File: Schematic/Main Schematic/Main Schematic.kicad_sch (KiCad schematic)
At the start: 7 parts, among them J1 Conn_01x24_Socket, J10 Conn_01x08_Pin, J3 Conn_01x24_Socket, J8 Conn_01x24_Pin, J9 Conn_01x24_Pin, SW1 SW_Push

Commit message: Updated the pcb
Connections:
- net RXD: now also J3.18 (Pin_18), J8.18 (Pin_18); no longer J3.19 (Pin_19), J8.19 (Pin_19)
- net TXD: now also J3.19 (Pin_19), J8.19 (Pin_19); no longer J3.18 (Pin_18), J8.18 (Pin_18)
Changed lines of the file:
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@@
     )
   )
-  (label "TXD" (at 253.9492 74.2696 0) (fields_autoplaced)
+  (label "TXD" (at 253.9492 76.8096 0) (fields_autoplaced)
     (effects (font (size 1.27 1.27)) (justify left bottom))
   )
@@
     (effects (font (size 1.27 1.27)) (justify left bottom))
   )
-  (label "RXD" (at 239.268 76.6572 0) (fields_autoplaced)
+  (label "RXD" (at 239.268 74.1172 0) (fields_autoplaced)
     (effects (font (size 1.27 1.27)) (justify left bottom))
   )
@@
     (effects (font (size 1.27 1.27)) (justify right bottom))
   )
-  (label "TXD" (at 239.268 74.1172 0) (fields_autoplaced)
-    (effects (font (size 1.27 1.27)) (justify left bottom))
-  )
-  (label "RXD" (at 253.9492 76.8096 0) (fields_autoplaced)
-    (effects (font (size 1.27 1.27)) (justify left bottom))
-  )
+  (label "TXD" (at 239.268 76.6572 0) (fields_autoplaced)
+    (effects (font (size 1.27 1.27)) (justify left bottom))
+  )
+  (label "RXD" (at 253.9492 74.2696 0) (fields_autoplaced)
+    (effects (font (size 1.27 1.27)) (justify left bottom))
+  )

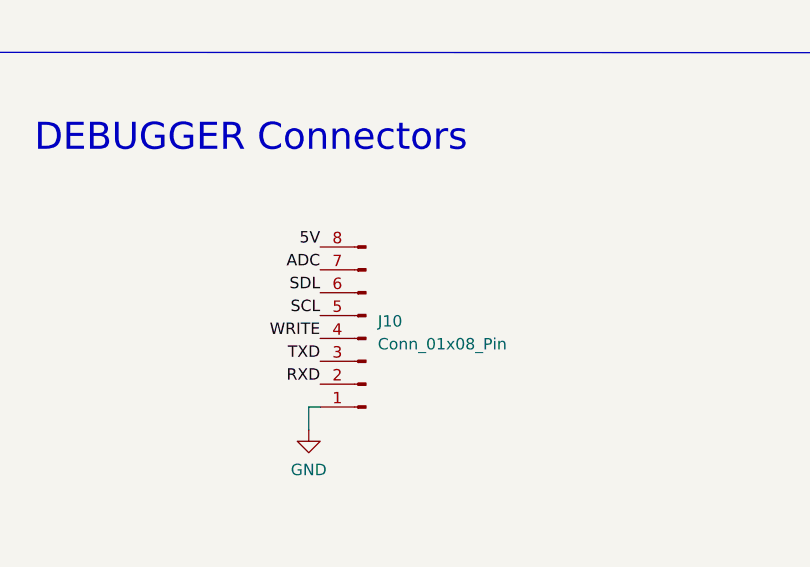
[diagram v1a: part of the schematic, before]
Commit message: Added more led for visual indications, also changed debugger pins to 9 pins for 3.3v pin
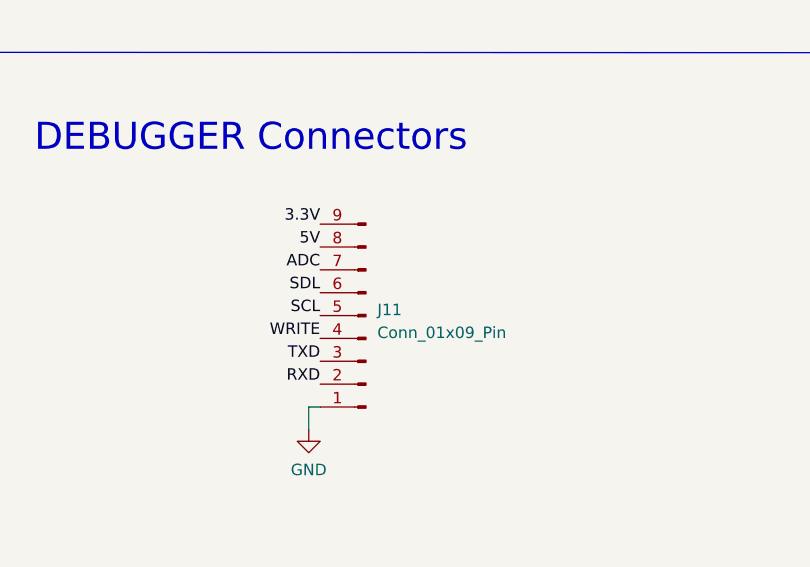
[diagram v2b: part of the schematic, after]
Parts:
- removed J10: Conn_01x08_Pin, Connector_PinHeader_2.54mm:PinHeader_1x08_P2.54mm_Vertical, symbol Connector:Conn_01x08_Pin
- added J11: Conn_01x09_Pin, Connector_PinHeader_2.54mm:PinHeader_1x09_P2.54mm_Vertical, symbol Connector:Conn_01x09_Pin
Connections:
- net 3.3V: now also J11.9 (Pin_9)
- net 5V: now also J11.8 (Pin_8)
- net ADC: now also J11.7 (Pin_7)
- net GND: now also J11.1 (Pin_1)
- net RXD: now also J11.2 (Pin_2)
- net SCL: now also J11.5 (Pin_5)
- net SDL: now also J11.6 (Pin_6)
- net TXD: now also J11.3 (Pin_3)
- net WRITE: now also J11.4 (Pin_4)
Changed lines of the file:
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@@
     )
+  )
+  (label "3.3V" (at 226.06 127 180) (fields_autoplaced)
+    (effects (font (size 1.27 1.27)) (justify right bottom))
   )
   (label "PB5" (at 253.9492 48.8696 0) (fields_autoplaced)
@@
         (path "/81c41bad-bb43-41af-b405-18d135a809b1"
           (reference "#PWR06") (unit 1)
-        )
-      )
-    )
-  )
-  (symbol (lib_id "Connector:Conn_01x08_Pin") (at 231.14 139.7 180) (unit 1)
-    (in_bom yes) (on_board yes) (dnp no) (fields_autoplaced)
-    (property "Reference" "J10" (at 232.4608 137.795 0)
-      (effects (font (size 1.27 1.27)) (justify right))
-    )
-    (property "Value" "Conn_01x08_Pin" (at 232.4608 140.335 0)
-      (effects (font (size 1.27 1.27)) (justify right))
-    )
-    (property "Footprint" "Connector_PinHeader_2.54mm:PinHeader_1x08_P2.54mm_Vertical" (at 231.14 139.7 0)
-      (effects (font (size 1.27 1.27)) hide)
-    )
-    (property "Datasheet" "~" (at 231.14 139.7 0)
-      (effects (font (size 1.27 1.27)) hide)
-    )
-    (pin "1")
-    (pin "2")
-    (pin "3")
-    (pin "4")
-    (pin "5")
-    (pin "6")
-    (pin "7")
-    (pin "8")
-    (instances
-      (project "Main Schematic"
-        (path "/81c41bad-bb43-41af-b405-18d135a809b1"
-          (reference "J10") (unit 1)
         )
       )
@@
         )
       )
+    )
+  )
+  (symbol (lib_id "Connector:Conn_01x09_Pin") (at 231.14 137.16 180) (unit 1)
+    (in_bom yes) (on_board yes) (dnp no) (fields_autoplaced)
+    (property "Reference" "J11" (at 232.41 136.525 0)
+      (effects (font (size 1.27 1.27)) (justify right))
+    )
+    (property "Value" "Conn_01x09_Pin" (at 232.41 139.065 0)
+      (effects (font (size 1.27 1.27)) (justify right))
+    )
+    (property "Footprint" "Connector_PinHeader_2.54mm:PinHeader_1x09_P2.54mm_Vertical" (at 231.14 137.16 0)
+      (effects (font (size 1.27 1.27)) hide)
+    )
+    (property "Datasheet" "~" (at 231.14 137.16 0)
+      (effects (font (size 1.27 1.27)) hide)
+    )
+    (pin "1")
+    (pin "2")
+    (pin "3")
+    (pin "4")
+    (pin "5")
+    (pin "6")
+    (pin "7")
+    (pin "8")
+    (pin "9")
+    (instances
+      (project "Main Schematic"
+        (path "/81c41bad-bb43-41af-b405-18d135a809b1"
+          (reference "J11") (unit 1)
+        )
+      )

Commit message: Design done
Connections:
- net GND: now also J1.8 (Pin_8), J9.8 (Pin_8)
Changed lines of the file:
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@@
-    (stroke (width 0) (type default))
-  )
-  (wire (pts (xy 193.294 48.768) (xy 207.518 48.768))
     (stroke (width 0) (type default))
   )
@@
     )
   )
+  (label "GND" (at 193.294 48.768 0) (fields_autoplaced)
+    (effects (font (size 1.27 1.27)) (justify left bottom))
+  )
   (label "OS" (at 77.8256 114.7572 0) (fields_autoplaced)
     (effects (font (size 1.27 1.27)) (justify left bottom))
@@
   (label "3.3V" (at 63.8048 97.7392 0) (fields_autoplaced)
     (effects (font (size 1.27 1.27)) (justify left bottom))
+  )
+  (label "GND" (at 207.518 48.768 180) (fields_autoplaced)
+    (effects (font (size 1.27 1.27)) (justify right bottom))
   )
   (label "BOOT" (at 239.014 41.0464 0) (fields_autoplaced)
@@
       (effects (font (size 1.27 1.27)))
     )
-    (property "Value" "Conn_01x24_Pin" (at 188.849 29.9212 0)
+    (property "Value" "Conn_01x24_Pin" (at 188.1124 24.8412 0)
       (effects (font (size 1.27 1.27)))
     )

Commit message: Design part Done
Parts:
- R1: footprint Resistor_SMD:R_1206_3216Metric -> Local_Footprints:R0805
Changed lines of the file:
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@@
       (effects (font (size 1.27 1.27)) (justify left))
     )
-    (property "Footprint" "Resistor_SMD:R_1206_3216Metric" (at 266.192 46.4312 90)
+    (property "Footprint" "Local_Footprints:R0805" (at 266.192 46.4312 90)
       (effects (font (size 1.27 1.27)) hide)
     )
